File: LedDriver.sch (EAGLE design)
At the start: 18 parts, among them IC1 CAT4101, IC2 CAT4101, X1 MKDSN1,5/3-5,08, X2 MKDSN1,5/4-5,08

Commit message: vwersion 1.0
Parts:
- C1: value (none) -> 10u; device rcl:CPOL-EUE3.5-8 -> rcl:C-EUC1210
- C2, C3: value (none) -> 100n
- D1, D2, D3: value (none) -> 5.6V; device diode:ZENER-DIODEDO35Z10 -> diode:ZENER-DIODESOD80C
- R1, R2, R3: value (none) -> 5k
- R4, R5: value (none) -> 2.7k
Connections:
- net GND: now also C1.2, X2-1.KL; no longer C1.-, X2-4.KL
- net N$3: now also X2-3.KL; no longer X2-2.KL
- net N$5: now also X2-2.KL; no longer X2-3.KL
- net VCC: now also C1.1, X2-4.KL; no longer C1.+, X2-1.KL
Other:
- moved on the sheet: X2-1, X2-2, X2-3, X2-4

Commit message: added pull up resistors for enable pin
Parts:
- added R6, R7: 100k, rcl:R-EU_R0603
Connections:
- net N$7: now also R6.1
- net N$8: now also R7.1
- net N$9: now also R6.2, R7.2
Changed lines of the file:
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@@
 </variantdefs>
 <classes>
-<class number="0" name="default" width="0" drill="0">
+<class number="0" name="default" width="0.4064" drill="0">
 </class>
 <class number="1" name="VCC" width="0.762" drill="0">
@@
 <part name="D3" library="diode" deviceset="ZENER-DIODE" device="SOD80C" value="5.6V"/>
 <part name="C1" library="rcl" deviceset="C-EU" device="C1210" value="10u"/>
+<part name="R6" library="rcl" deviceset="R-EU_" device="R0603" value="100k"/>
+<part name="R7" library="rcl" deviceset="R-EU_" device="R0603" value="100k"/>
 </parts>
 <sheets>
@@
 <instance part="D3" gate="G$1" x="-25.4" y="-5.08" rot="R90"/>
 <instance part="C1" gate="G$1" x="-35.56" y="68.58"/>
+<instance part="R6" gate="G$1" x="10.16" y="50.8" rot="R180"/>
+<instance part="R7" gate="G$1" x="10.16" y="17.78" rot="R180"/>
 </instances>
 <busses>
@@
 <pinref part="IC1" gate="G$1" pin="EN/PWM"/>
 <wire x1="-2.54" y1="53.34" x2="15.24" y2="53.34" width="0.1524" layer="91"/>
+<pinref part="R6" gate="G$1" pin="1"/>
+<wire x1="15.24" y1="50.8" x2="15.24" y2="53.34" width="0.1524" layer="91"/>
+<junction x="15.24" y="53.34"/>
 </segment>
 </net>
@@
 <wire x1="15.24" y1="20.32" x2="-2.54" y2="20.32" width="0.1524" layer="91"/>
 <wire x1="-2.54" y1="20.32" x2="-2.54" y2="-10.16" width="0.1524" layer="91"/>
+<pinref part="R7" gate="G$1" pin="1"/>
+<wire x1="15.24" y1="20.32" x2="15.24" y2="17.78" width="0.1524" layer="91"/>
+<junction x="15.24" y="20.32"/>
 </segment>
 </net>
@@
 <pinref part="Q1" gate="G$1" pin="S"/>
 <pinref part="IC1" gate="G$1" pin="VIN"/>
-<wire x1="15.24" y1="55.88" x2="2.54" y2="55.88" width="0.1524" layer="91"/>
+<wire x1="15.24" y1="55.88" x2="5.08" y2="55.88" width="0.1524" layer="91"/>
+<wire x1="5.08" y1="55.88" x2="2.54" y2="55.88" width="0.1524" layer="91"/>
 <wire x1="2.54" y1="55.88" x2="-10.16" y2="55.88" width="0.1524" layer="91"/>
 <wire x1="-10.16" y1="55.88" x2="-10.16" y2="58.42" width="0.1524" layer="91"/>
@@
 <pinref part="IC2" gate="G$1" pin="VIN"/>
 <wire x1="2.54" y1="48.26" x2="2.54" y2="55.88" width="0.1524" layer="91"/>
-<wire x1="15.24" y1="22.86" x2="2.54" y2="22.86" width="0.1524" layer="91"/>
+<wire x1="15.24" y1="22.86" x2="5.08" y2="22.86" width="0.1524" layer="91"/>
+<wire x1="5.08" y1="22.86" x2="2.54" y2="22.86" width="0.1524" layer="91"/>
 <wire x1="2.54" y1="22.86" x2="0" y2="22.86" width="0.1524" layer="91"/>
 <wire x1="0" y1="22.86" x2="0" y2="48.26" width="0.1524" layer="91"/>
@@
 <wire x1="2.54" y1="12.7" x2="2.54" y2="22.86" width="0.1524" layer="91"/>
 <junction x="2.54" y="22.86"/>
-</segment>
-</net>
+<pinref part="R7" gate="G$1" pin="2"/>
+<wire x1="5.08" y1="17.78" x2="5.08" y2="22.86" width="0.1524" layer="91"/>
+<pinref part="R6" gate="G$1" pin="2"/>
+<wire x1="5.08" y1="50.8" x2="5.08" y2="55.88" width="0.1524" layer="91"/>
+<junction x="5.08" y="55.88"/>
+<junction x="5.08" y="22.86"/>
+</segment>
+</net>

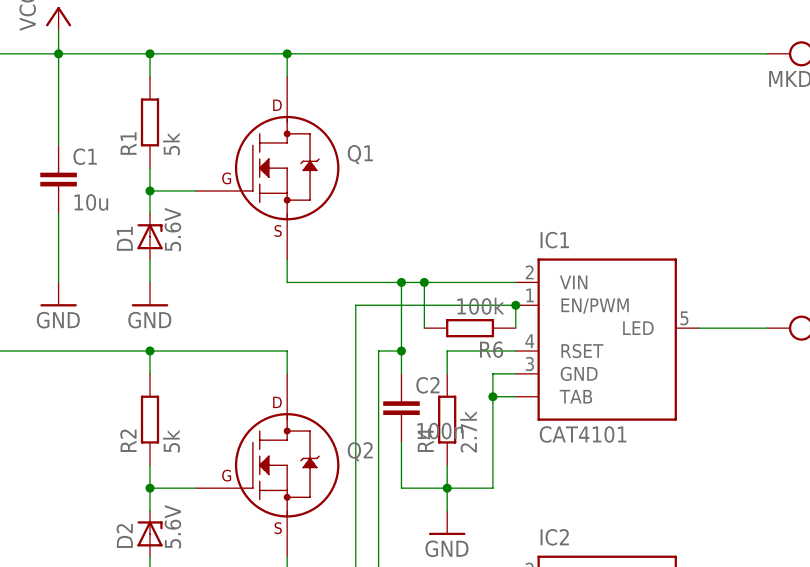
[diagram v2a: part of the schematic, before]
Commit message: added reverse polarity protection diode
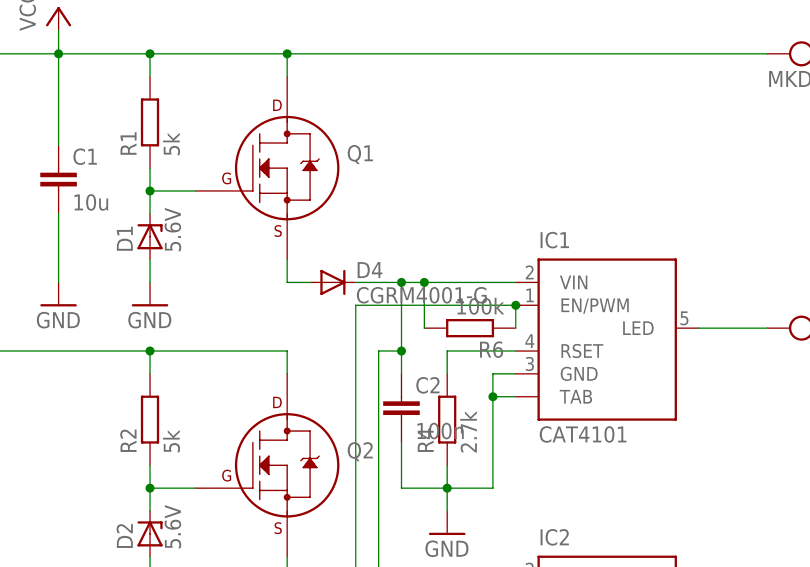
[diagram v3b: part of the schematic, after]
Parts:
- added D4: CGRM4001-G, diode:CGRM4001-G
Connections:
- new net N$2: D4.A, Q1.S
- net N$9: now also D4.C; no longer Q1.S
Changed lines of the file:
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@@
 <part name="R6" library="rcl" deviceset="R-EU_" device="R0603" value="100k"/>
 <part name="R7" library="rcl" deviceset="R-EU_" device="R0603" value="100k"/>
+<part name="D4" library="diode" deviceset="CGRM400*-G" device="" technology="1"/>
 </parts>
 <sheets>
@@
 <instance part="R6" gate="G$1" x="10.16" y="50.8" rot="R180"/>
 <instance part="R7" gate="G$1" x="10.16" y="17.78" rot="R180"/>
+<instance part="D4" gate="G$1" x="-5.08" y="55.88"/>
 </instances>
 <busses>
@@
 <net name="N$9" class="0">
 <segment>
-<pinref part="Q1" gate="G$1" pin="S"/>
 <pinref part="IC1" gate="G$1" pin="VIN"/>
 <wire x1="15.24" y1="55.88" x2="5.08" y2="55.88" width="0.1524" layer="91"/>
 <wire x1="5.08" y1="55.88" x2="2.54" y2="55.88" width="0.1524" layer="91"/>
-<wire x1="2.54" y1="55.88" x2="-10.16" y2="55.88" width="0.1524" layer="91"/>
-<wire x1="-10.16" y1="55.88" x2="-10.16" y2="58.42" width="0.1524" layer="91"/>
 <pinref part="C2" gate="G$1" pin="1"/>
 <wire x1="2.54" y1="45.72" x2="2.54" y2="48.26" width="0.1524" layer="91"/>
-<junction x="2.54" y="55.88"/>
 <pinref part="IC2" gate="G$1" pin="VIN"/>
 <wire x1="2.54" y1="48.26" x2="2.54" y2="55.88" width="0.1524" layer="91"/>
@@
 <junction x="5.08" y="55.88"/>
 <junction x="5.08" y="22.86"/>
+<pinref part="D4" gate="G$1" pin="C"/>
+<wire x1="-2.54" y1="55.88" x2="2.54" y2="55.88" width="0.1524" layer="91"/>
+<junction x="2.54" y="55.88"/>
 </segment>
 </net>
@@
 </segment>
 </net>
+<net name="N$2" class="0">
+<segment>
+<pinref part="Q1" gate="G$1" pin="S"/>
+<wire x1="-10.16" y1="58.42" x2="-10.16" y2="55.88" width="0.1524" layer="91"/>
+<pinref part="D4" gate="G$1" pin="A"/>
+<wire x1="-10.16" y1="55.88" x2="-7.62" y2="55.88" width="0.1524" layer="91"/>
+</segment>
+</net>
